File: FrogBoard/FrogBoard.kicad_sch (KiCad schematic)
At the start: 33 parts, among them J1 Conn_01x10, J2 Conn_01x04, J3 USB_B_Micro, J4 Stickbox, U1 STM32L432KBUx, U2 USBLC6-2P6, U3 MCP1700T-3302E, U4 EMS3900

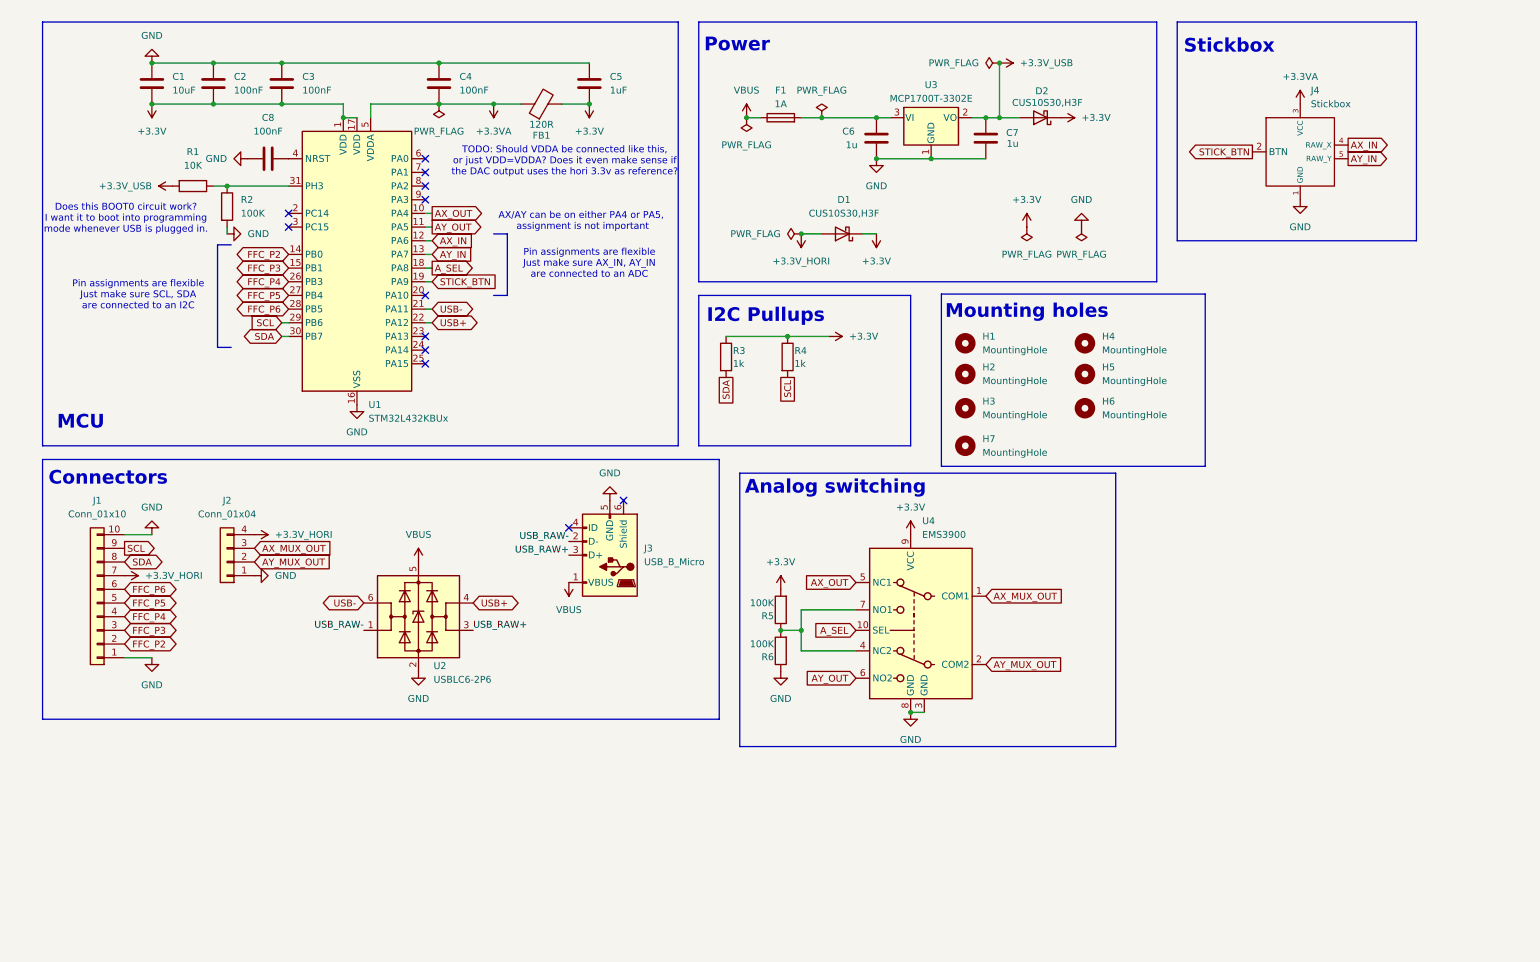
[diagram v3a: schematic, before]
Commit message: Cleaned up power filtering, fixed broken symbol and foorpting for mux, and started layout work
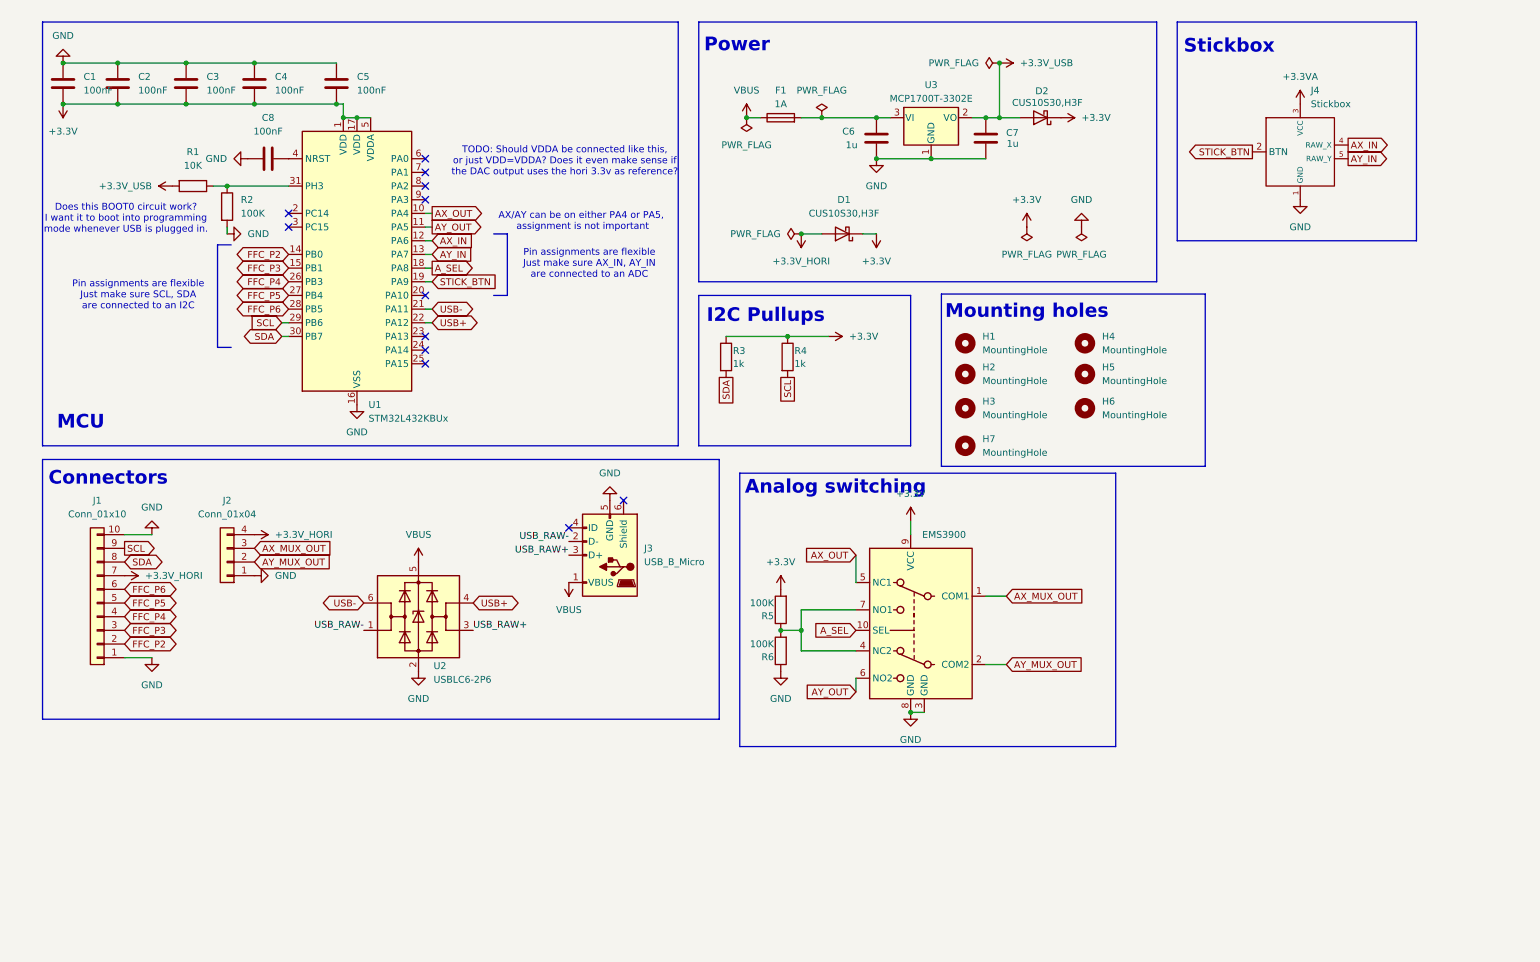
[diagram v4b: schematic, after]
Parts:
- removed FB1: 120R, Resistor_SMD:R_0805_2012Metric_Pad1.20x1.40mm_HandSolder, symbol Device:FerriteBead
- C1: value 10uF -> 100nF; footprint Capacitor_SMD:C_0805_2012Metric_Pad1.18x1.45mm_HandSolder -> Capacitor_SMD:C_0603_1608Metric_Pad1.08x0.95mm_HandSolder
- C5: value 1uF -> 100nF; footprint Capacitor_SMD:C_0805_2012Metric_Pad1.18x1.45mm_HandSolder -> Capacitor_SMD:C_0603_1608Metric_Pad1.08x0.95mm_HandSolder
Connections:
- net +3.3V: now also C4.2, U1.5 (VDDA)
- net +3.3VA: no longer C4.2, U1.5 (VDDA)
- net GND: no longer U4.11 (GND)
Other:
- moved on the sheet: C2, C3, C4

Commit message: routed the power section, places most ofthe components. Test points still to be added
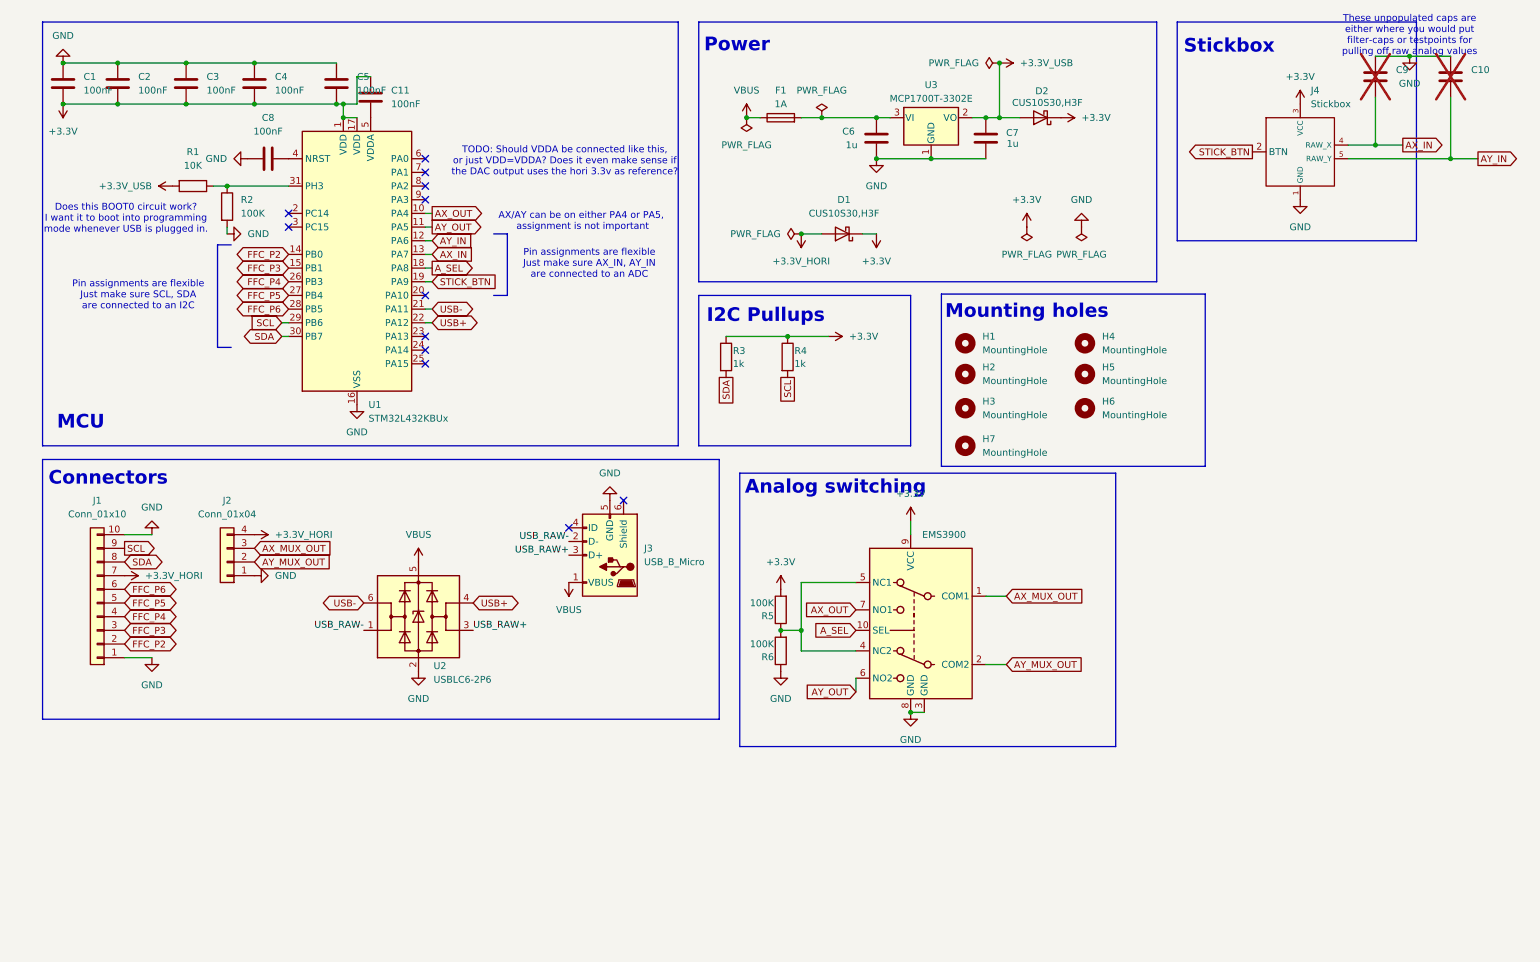
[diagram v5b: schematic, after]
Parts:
- added C10, C9: ~, Capacitor_THT:C_Disc_D3.0mm_W1.6mm_P2.50mm, symbol Device:C
- added C11: 100nF, Capacitor_SMD:C_0603_1608Metric_Pad1.08x0.95mm_HandSolder, symbol Device:C
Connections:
- net +3.3VA is gone; now on net +3.3V: J4.3 (VCC)
- net +3.3V: now also C11.1; no longer U1.5 (VDDA)
- net AX_IN: now also U1.13 (PA7), C9.2; no longer U1.12 (PA6)
- net AX_OUT: now also U4.7 (NO1); no longer U4.5 (NC1)
- net AY_IN: now also U1.12 (PA6), C10.2; no longer U1.13 (PA7)
- net GND: now also C10.1, C9.1
- net at R5.1, R6.2, U4.4 (NC2): now also U4.5 (NC1); no longer U4.7 (NO1)
- new net: C11.2, U1.5 (VDDA)
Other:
- note added: "These unpopulated caps are either where you would put filter-caps or testpoints for pulling off raw analog values"

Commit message: Switch to BL1555 analog chip
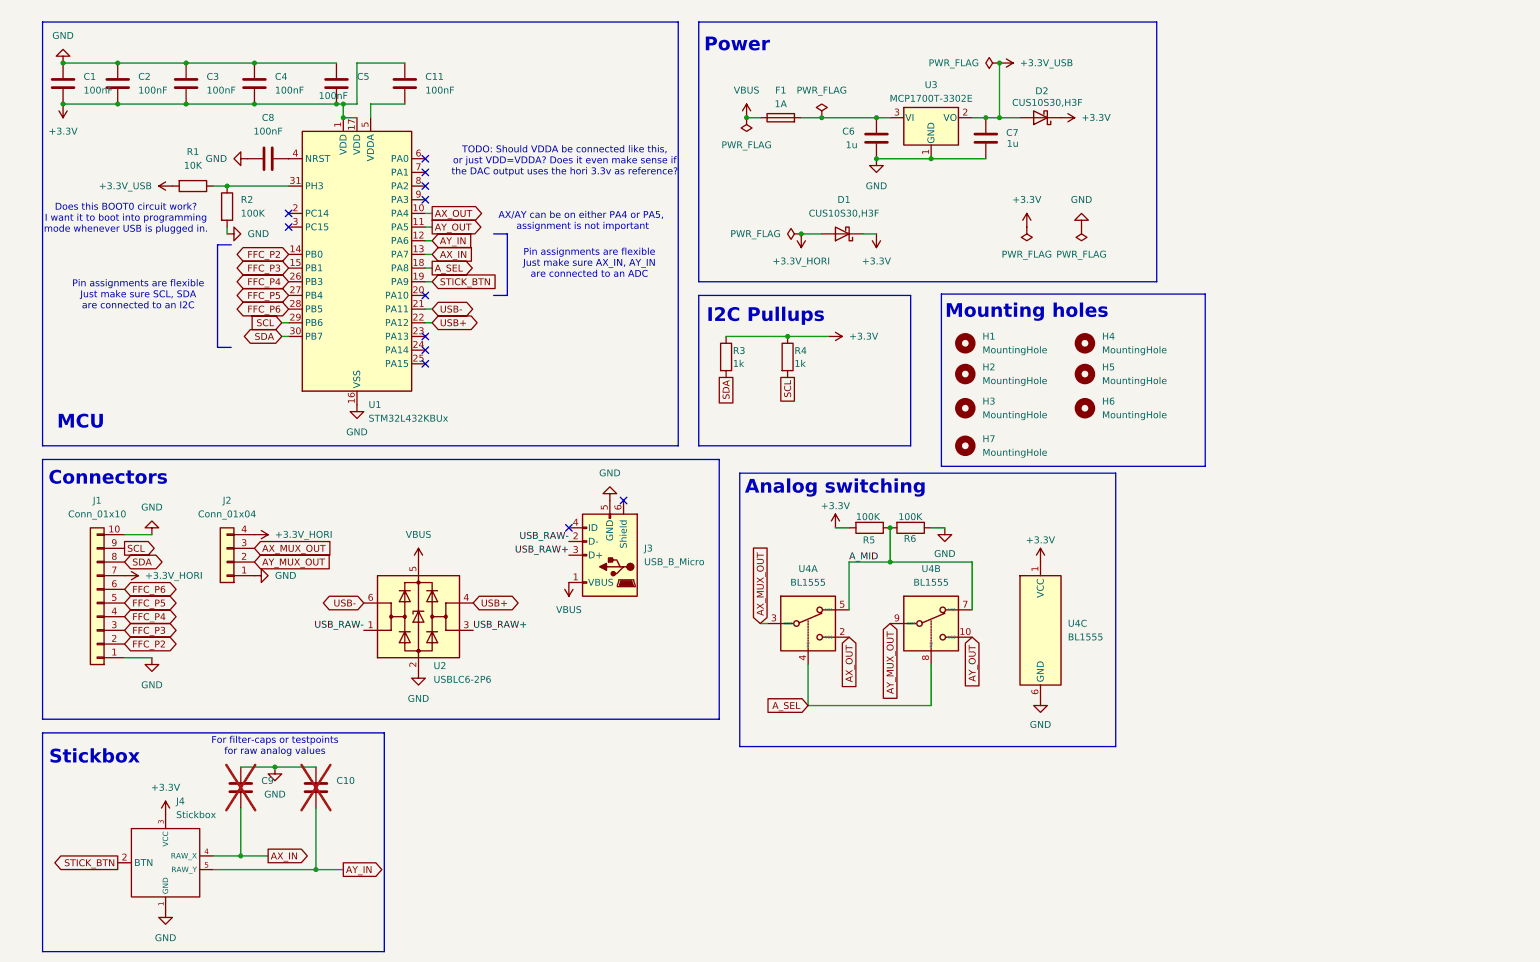
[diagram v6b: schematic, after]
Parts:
- removed U4: EMS3900, Package_DFN_QFN:UQFN-10_1.4x1.8mm_P0.4mm, symbol FrogBoard:EMS3900
- added U4: BL1555, Package_SO:MSOP-10_3x3mm_P0.5mm, symbol FrogBoard:BL1555
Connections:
- net +3.3V: now also U4.1 (VCC)
- net AX_MUX_OUT: now also U4.3 (COM1)
- net AX_OUT: now also U4.2 (NO1)
- net AY_MUX_OUT: now also U4.9 (COM2)
- net AY_OUT: now also U4.10 (NO2)
- net A_SEL: now also U4.4 (IN1), U4.8 (IN2)
- net GND: now also U4.6 (GND)
- net A_MID: now reaches R5.1, R6.2
- net A_MID: now also U4.5 (NC1), U4.7 (NC2)
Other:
- note added: "For filter-caps or testpoints for raw analog values"
- note removed: "These unpopulated caps are either where you would put filter-caps or testpoints for pulling off raw analog values"
- moved on the sheet: C10, C11, C9, J4, R5, R6

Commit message: first pass at layout
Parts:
- added J5: Conn_01x03_Socket, Connector_PinHeader_1.00mm:PinHeader_1x03_P1.00mm_Vertical, symbol Connector:Conn_01x03_Socket
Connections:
- net +3.3V: now also C11.2, U1.5 (VDDA), J5.3 (Pin_3); no longer C11.1
- net AX_MUX_OUT: now also U4.9 (COM2); no longer U4.3 (COM1)
- net AX_OUT: now also U4.10 (NO2); no longer U4.2 (NO1)
- net AY_MUX_OUT: now also U4.3 (COM1); no longer U4.9 (COM2)
- net AY_OUT: now also U4.2 (NO1); no longer U4.10 (NO2)
- net FFC_P2: now also U1.27 (PB4); no longer U1.14 (PB0)
- net FFC_P3: now also U1.28 (PB5); no longer U1.15 (PB1)
- net FFC_P5: now also U1.15 (PB1); no longer U1.27 (PB4)
- net FFC_P6: now also U1.14 (PB0); no longer U1.28 (PB5)
- net GND: now also C11.1, J5.1 (Pin_1)
- net BOOT_SEL: now reaches R1.1, R2.1, U1.31 (PH3)
- net BOOT_SEL: now also J5.2 (Pin_2)
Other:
- moved on the sheet: C5, R1, U4A, U4B

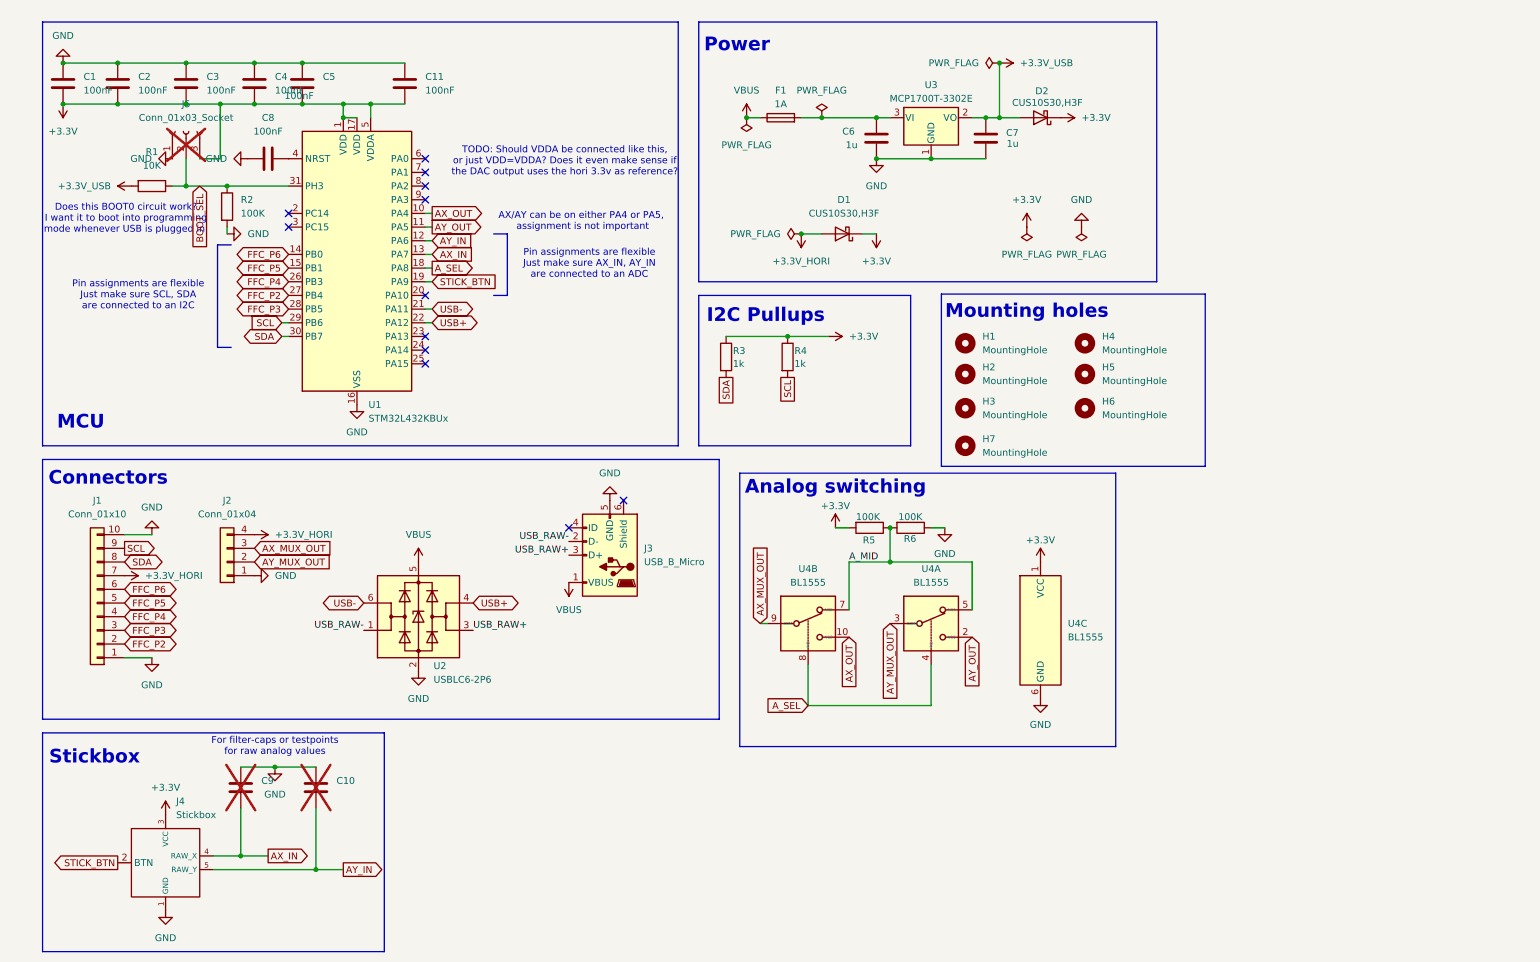
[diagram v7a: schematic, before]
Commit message: Add NRST header, clean up silkscreens
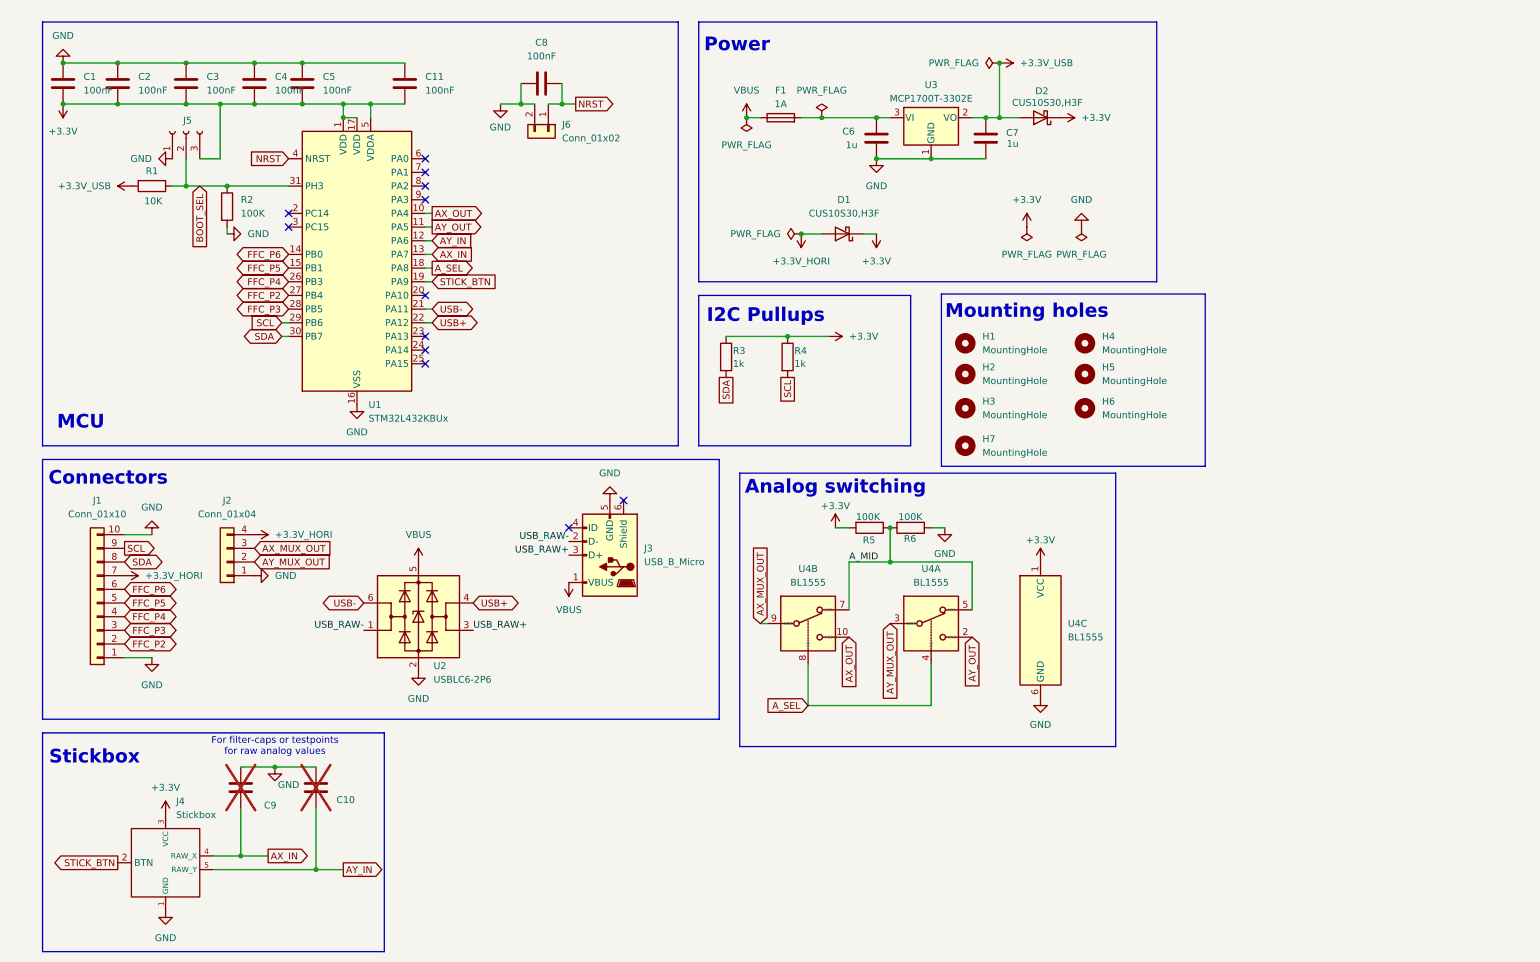
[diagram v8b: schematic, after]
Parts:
- added J6: Conn_01x02, Connector_PinHeader_1.00mm:PinHeader_1x02_P1.00mm_Vertical, symbol Connector_Generic:Conn_01x02
- J5: now fitted
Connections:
- net GND: now also J6.2 (Pin_2)
- net NRST: now reaches C8.2, U1.4 (NRST)
- net NRST: now also J6.1 (Pin_1)
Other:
- note removed: "AX/AY can be on either PA4 or PA5, assignment is not important"
- note removed: "Does this BOOT0 circuit work? I want it to boot into programming mode whenever USB is plugged in."
- note removed: "Pin assignments are flexible Just make sure AX_IN, AY_IN are connected to an ADC"
- note removed: "Pin assignments are flexible Just make sure SCL, SDA are connected to an I2C"
- note removed: "TODO: Should VDDA be connected like this, or just VDD=VDDA? Does it even make sense if the DAC output uses the hori 3.3v as reference?"
- moved on the sheet: C8
